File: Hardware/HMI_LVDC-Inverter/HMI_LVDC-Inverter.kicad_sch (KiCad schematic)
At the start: 1 part, among them J10 Conn_01x06_Pin

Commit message: Terminado el esquemático del HMI
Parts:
- removed J10: Conn_01x06_Pin, symbol Connector:Conn_01x06_Pin
- added J1: Conn_01x02, Connector_Hirose:Hirose_DF13-02P-1.25DS_1x02_P1.25mm_Horizontal, symbol Connector_Generic:Conn_01x02
- added J2: Conn_01x09_Pin, Connector_Phoenix_SPT:PhoenixContact_SPT_2.5_9-V-5.0-EX_1x09_P5.0mm_Vertical, symbol Connector:Conn_01x09_Pin
- added J3, J4, J5: Conn_01x05, Connector_PinHeader_1.00mm:PinHeader_1x05_P1.00mm_Vertical, symbol Connector_Generic:Conn_01x05
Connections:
- net GND: now also J3.5 (Pin_5), J4.2 (Pin_2), J5.1 (Pin_1)
- new net +12V_ISO: J1.1 (Pin_1)
- new net +3.3V: J4.5 (Pin_5)
- new net +5V: J4.1 (Pin_1)
- new net GND_ISO: J1.2 (Pin_2)
- new net MCU/ESP_EN: J3.3 (Pin_3)
- new net MCU/ESP_PROG: J3.4 (Pin_4)
- new net MCU/MISO: J5.4 (Pin_4)
- new net MCU/MOSI: J5.5 (Pin_5)
- new net MCU/NSS: J5.2 (Pin_2)
- new net MCU/RXD0_prog: J3.1 (Pin_1)
- new net MCU/SCK: J5.3 (Pin_3)
- new net MCU/TXD0_prog: J3.2 (Pin_2)
- new net MCU/VSens_Corriente: J4.3 (Pin_3)
- new net MCU/Vsens_HV: J4.4 (Pin_4)
- new net Perifericos/FREQ_SEL_1_ISO: J2.6 (Pin_6)
- new net Perifericos/FREQ_SEL_2_ISO: J2.5 (Pin_5)
- new net Perifericos/FREQ_SEL_3_ISO: J2.4 (Pin_4)
- new net Perifericos/FREQ_SEL_4_ISO: J2.3 (Pin_3)
- new net Perifericos/RELAY_COM: J2.8 (Pin_8)
- new net Perifericos/RELAY_NC: J2.7 (Pin_7)
- new net Perifericos/RELAY_NO: J2.9 (Pin_9)
- new net Perifericos/START_CTRL_ISO: J2.2 (Pin_2)
- new net Perifericos/STOP_BUTTON_ISO: J2.1 (Pin_1)
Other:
- sheet Fuentes ports: added none; removed 12V_test
- sheet MCU ports: added ESP_EN, ESP_PROG, FREQ_SEL_1, FREQ_SEL_2, FREQ_SEL_3, FREQ_SEL_4, MISO, MOSI, NSS, RELAY_CTRL, RXD0_prog, SCK, START_CTRL, STOP_BUTTON, TXD0_prog, V0-10V, VSens_Corriente, Vsens_HV; removed 12V_test, Inv_Rx, Inv_Tx, Touch_0, Touch_1, Touch_2, Touch_3, Touch_4, Touch_5
- sheet Perifericos ports: added FREQ_SEL_1, FREQ_SEL_1_ISO, FREQ_SEL_2, FREQ_SEL_2_ISO, FREQ_SEL_3, FREQ_SEL_3_ISO, FREQ_SEL_4, FREQ_SEL_4_ISO, RELAY_COM, RELAY_CTRL, RELAY_NC, RELAY_NO, START_CTRL, START_CTRL_ISO, STOP_BUTTON, STOP_BUTTON_ISO, V0-10V; removed Touch_0, Touch_1, Touch_2, Touch_3, Touch_4, Touch_5
- note added: "CONECTORES CON INVERTER"
- note removed: "CONECTOR CON INVERTER"

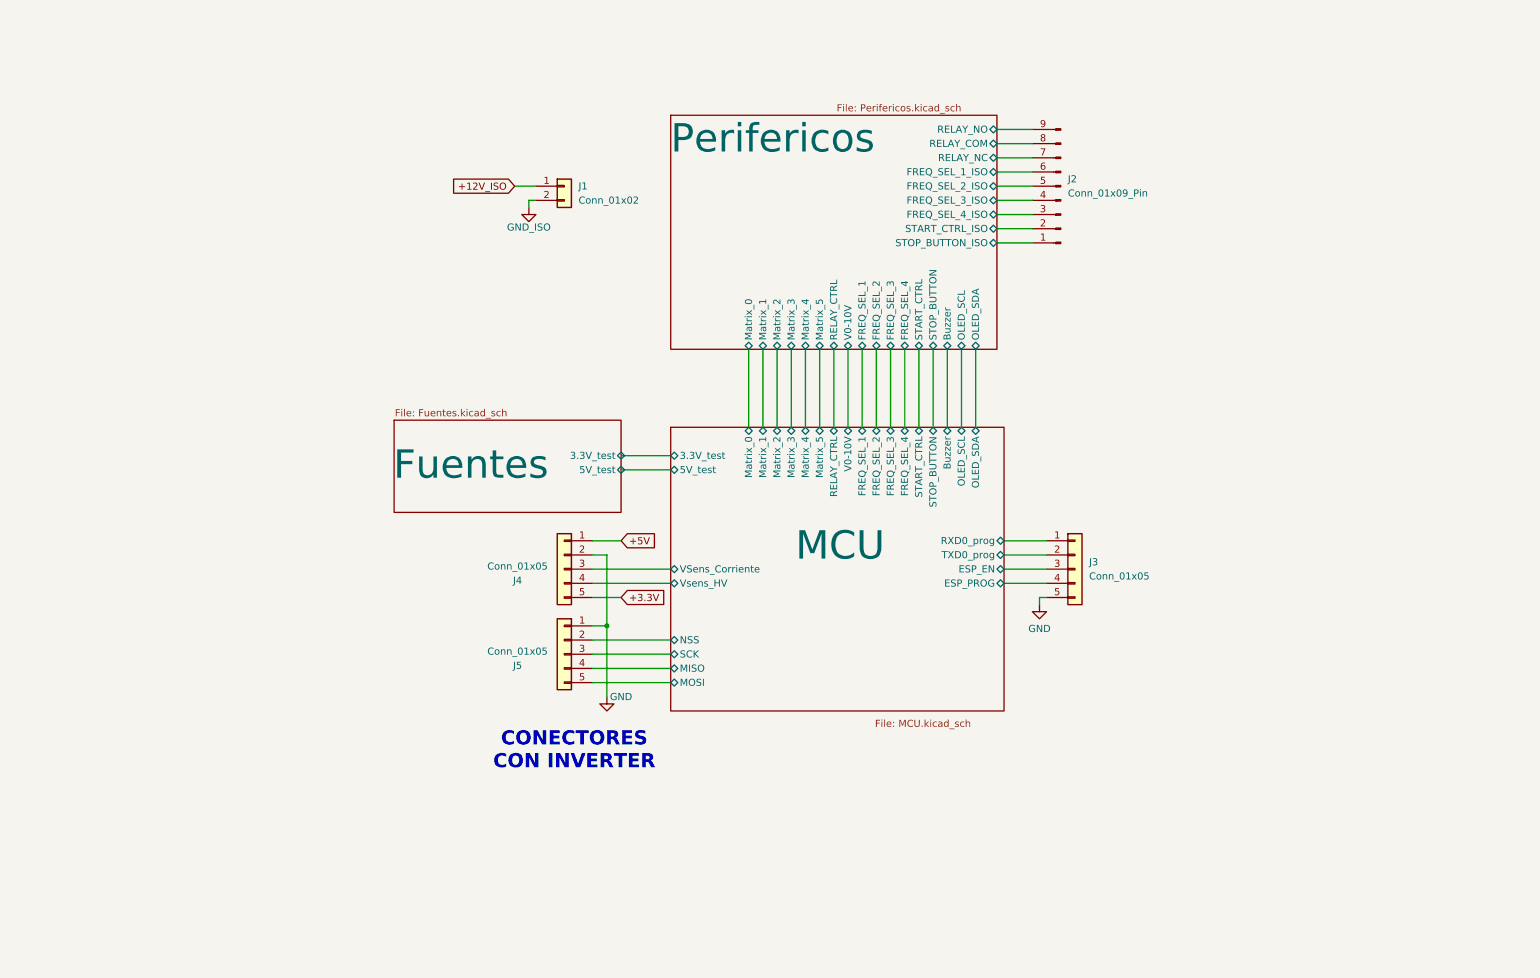
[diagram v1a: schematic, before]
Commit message: Avance con el esquemático, faltan definir algunas etiquetas que no las encontré
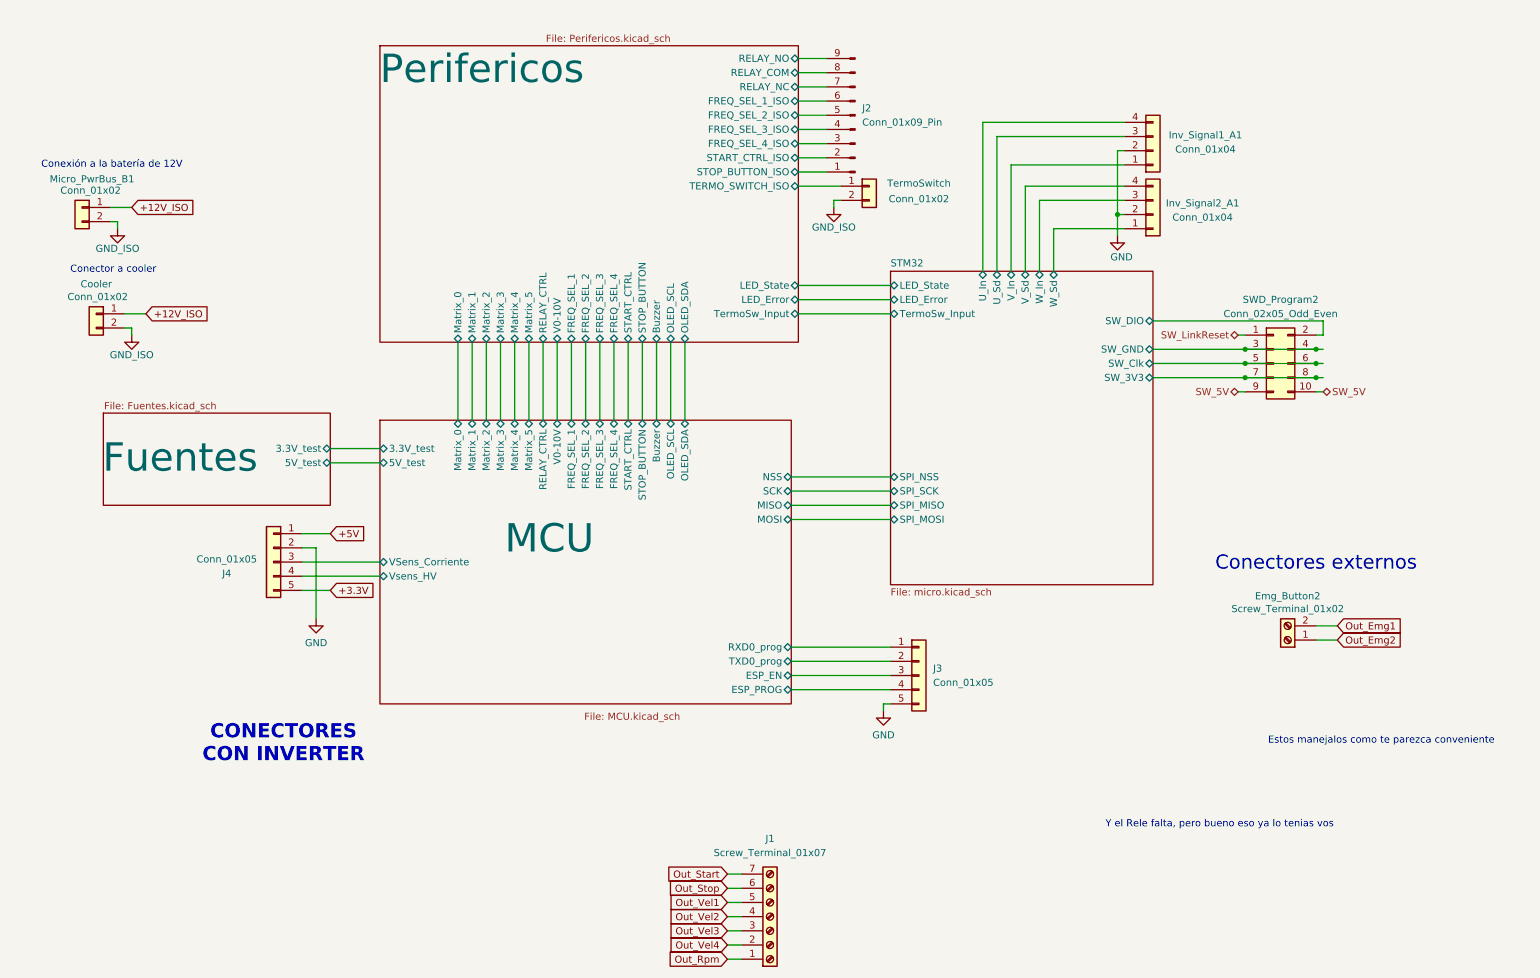
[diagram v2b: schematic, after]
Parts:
- removed J1: Conn_01x02, Connector_Hirose:Hirose_DF13-02P-1.25DS_1x02_P1.25mm_Horizontal, symbol Connector_Generic:Conn_01x02
- removed J5: Conn_01x05, Connector_PinHeader_1.00mm:PinHeader_1x05_P1.00mm_Vertical, symbol Connector_Generic:Conn_01x05
- added Cooler, TermoSwitch: Conn_01x02, Connector_Molex:Molex_KK-254_AE-6410-02A_1x02_P2.54mm_Vertical, symbol Connector_Generic:Conn_01x02
- added Emg_Button2: Screw_Terminal_01x02, TerminalBlock_Phoenix:TerminalBlock_Phoenix_MKDS-1,5-2_1x02_P5.00mm_Horizontal, symbol Connector:Screw_Terminal_01x02
- added Inv_Signal1_A1, Inv_Signal2_A1: Conn_01x04, Connector_Molex:Molex_KK-254_AE-6410-04A_1x04_P2.54mm_Vertical, symbol Connector_Generic:Conn_01x04
- added J1: Screw_Terminal_01x07, TerminalBlock_Phoenix:TerminalBlock_Phoenix_PT-1,5-7-5.0-H_1x07_P5.00mm_Horizontal, symbol Connector:Screw_Terminal_01x07
- added Micro_PwrBus_B1: Conn_01x02, Connector_Phoenix_MSTB:PhoenixContact_MSTBVA_2,5_2-G-5,08_1x02_P5.08mm_Vertical, symbol Connector_Generic:Conn_01x02
- added SWD_Program2: Conn_02x05_Odd_Even, Connector_IDC:IDC-Header_2x05_P2.54mm_Vertical_SMD, symbol Connector_Generic:Conn_02x05_Odd_Even
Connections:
- net +12V_ISO: now also Cooler.1 (Pin_1), Micro_PwrBus_B1.1 (Pin_1)
- net GND: now also Inv_Signal1_A1.2 (Pin_2), Inv_Signal2_A1.2 (Pin_2)
- net GND_ISO: now also Cooler.2 (Pin_2), Micro_PwrBus_B1.2 (Pin_2), TermoSwitch.2 (Pin_2)
- new net Out_Emg1: Emg_Button2.2 (Pin_2)
- new net Out_Emg2: Emg_Button2.1 (Pin_1)
- new net Out_Rpm: J1.1 (Pin_1)
- new net Out_Start: J1.7 (Pin_7)
- new net Out_Stop: J1.6 (Pin_6)
- new net Out_Vel1: J1.5 (Pin_5)
- new net Out_Vel2: J1.4 (Pin_4)
- new net Out_Vel3: J1.3 (Pin_3)
- new net Out_Vel4: J1.2 (Pin_2)
- new net Perifericos/TERMO_SWITCH_ISO: TermoSwitch.1 (Pin_1)
- new net STM32/SW_3V3: SWD_Program2.7 (Pin_7), SWD_Program2.8 (Pin_8)
- new net STM32/SW_Clk: SWD_Program2.5 (Pin_5), SWD_Program2.6 (Pin_6)
- new net STM32/SW_DIO: SWD_Program2.2 (Pin_2)
- new net STM32/SW_GND: SWD_Program2.3 (Pin_3), SWD_Program2.4 (Pin_4)
- new net STM32/U_In: Inv_Signal1_A1.4 (Pin_4)
- new net STM32/U_Sd: Inv_Signal1_A1.3 (Pin_3)
- new net STM32/V_In: Inv_Signal1_A1.1 (Pin_1)
- new net STM32/V_Sd: Inv_Signal2_A1.4 (Pin_4)
- new net STM32/W_In: Inv_Signal2_A1.3 (Pin_3)
- new net STM32/W_Sd: Inv_Signal2_A1.1 (Pin_1)
- new net SW_5V: SWD_Program2.10 (Pin_10), SWD_Program2.9 (Pin_9)
- new net SW_LinkReset: SWD_Program2.1 (Pin_1)
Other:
- added sheet STM32 (micro.kicad_sch)
- sheet Perifericos ports: added LED_Error, LED_State, TERMO_SWITCH_ISO, TermoSw_Input; removed none
- note added: "Conector a cooler"
- note added: "Conectores externos"
- note added: "Conexión a la batería de 12V"
- note added: "Estos manejalos como te parezca conveniente"
- note added: "Y el Rele falta, pero bueno eso ya lo tenias vos"
- moved on the sheet: J2, J3, J4

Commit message: Terminado todo el conexionado eléctrico esquemático
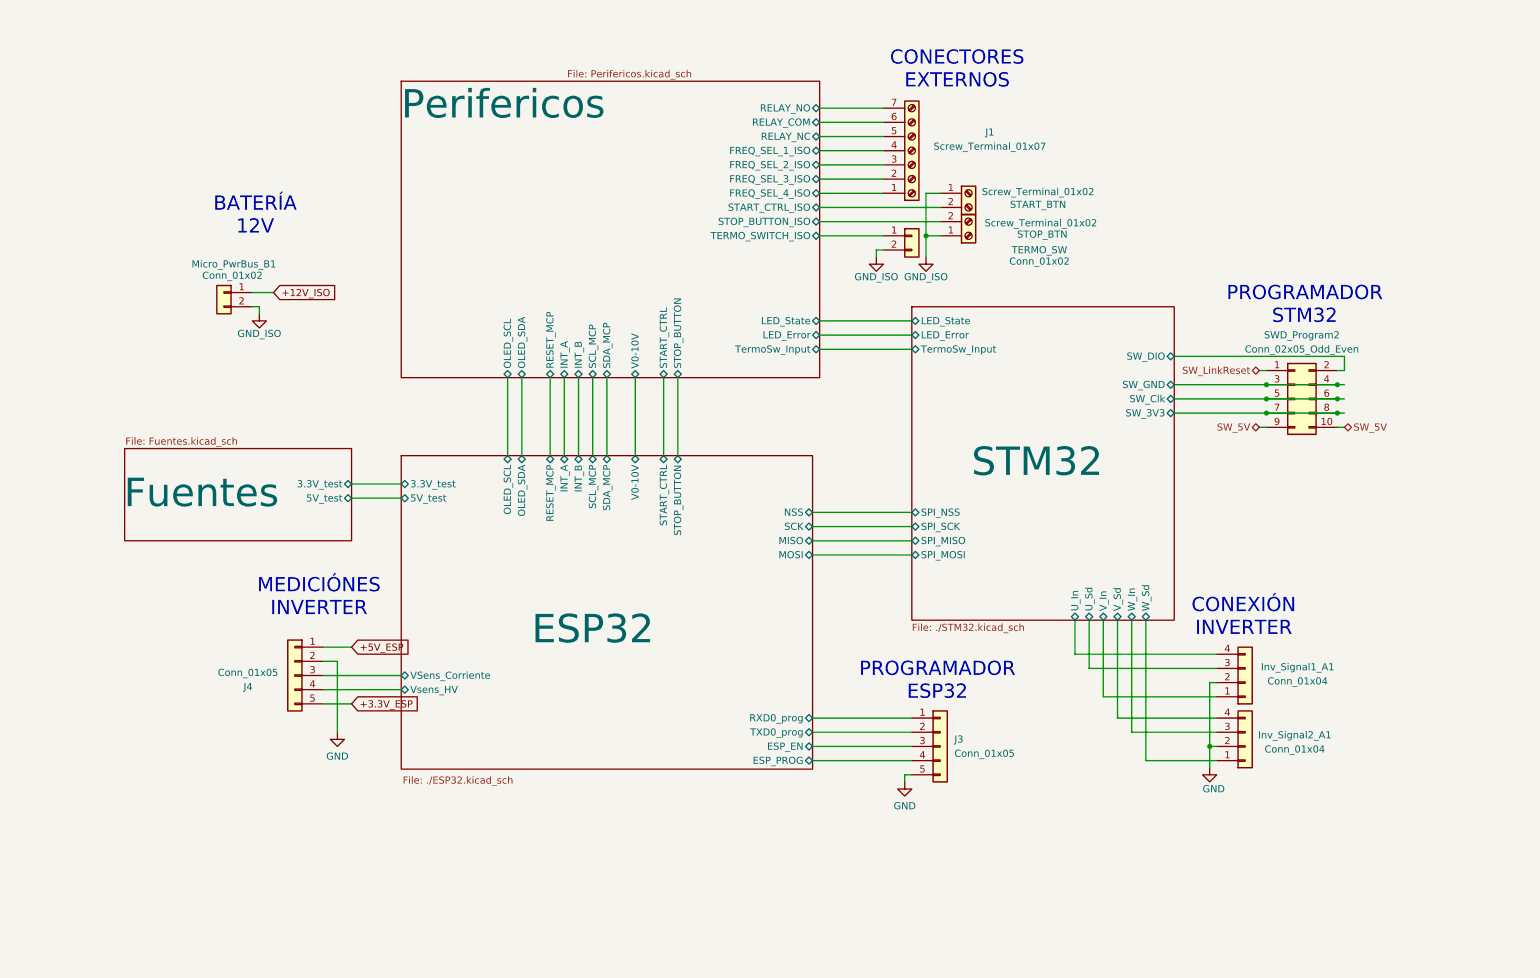
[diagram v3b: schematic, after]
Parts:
- removed Cooler: Conn_01x02, Connector_Molex:Molex_KK-254_AE-6410-02A_1x02_P2.54mm_Vertical, symbol Connector_Generic:Conn_01x02
- removed J2: Conn_01x09_Pin, Connector_Phoenix_SPT:PhoenixContact_SPT_2.5_9-V-5.0-EX_1x09_P5.0mm_Vertical, symbol Connector:Conn_01x09_Pin
- added STOP_BTN: Screw_Terminal_01x02, TerminalBlock_Phoenix:TerminalBlock_Phoenix_MKDS-1,5-2_1x02_P5.00mm_Horizontal, symbol Connector:Screw_Terminal_01x02
- renumbered Emg_Button2 to START_BTN, TermoSwitch to TERMO_SW
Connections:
- net Out_Emg1 is gone; now on net Perifericos/START_CTRL_ISO: START_BTN.2 (Pin_2)
- net Out_Emg2 is gone; now on net GND_ISO: START_BTN.1 (Pin_1)
- net Out_Rpm is gone; now on net Perifericos/FREQ_SEL_4_ISO: J1.1 (Pin_1)
- net Out_Start is gone; now on net Perifericos/RELAY_NO: J1.7 (Pin_7)
- net Out_Stop is gone; now on net Perifericos/RELAY_COM: J1.6 (Pin_6)
- net Out_Vel1 is gone; now on net Perifericos/RELAY_NC: J1.5 (Pin_5)
- net Out_Vel2 is gone; now on net Perifericos/FREQ_SEL_1_ISO: J1.4 (Pin_4)
- net Out_Vel3 is gone; now on net Perifericos/FREQ_SEL_2_ISO: J1.3 (Pin_3)
- net Out_Vel4 is gone; now on net Perifericos/FREQ_SEL_3_ISO: J1.2 (Pin_2)
- net GND_ISO: now also STOP_BTN.1 (Pin_1)
- net Perifericos/STOP_BUTTON_ISO: now also STOP_BTN.2 (Pin_2)
- net +3.3V renamed +3.3V_ESP
- net +5V renamed +5V_ESP
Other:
- sheet MCU renamed ESP32
- sheet ESP32: file MCU.kicad_sch -> ./ESP32.kicad_sch
- sheet ESP32 ports: added INT_A, INT_B, RESET_MCP, SCL_MCP, SDA_MCP; removed Buzzer, FREQ_SEL_1, FREQ_SEL_2, FREQ_SEL_3, FREQ_SEL_4, Matrix_0, Matrix_1, Matrix_2, Matrix_3, Matrix_4, Matrix_5, RELAY_CTRL
- sheet Perifericos ports: added INT_A, INT_B, RESET_MCP, SCL_MCP, SDA_MCP; removed Buzzer, FREQ_SEL_1, FREQ_SEL_2, FREQ_SEL_3, FREQ_SEL_4, Matrix_0, Matrix_1, Matrix_2, Matrix_3, Matrix_4, Matrix_5, RELAY_CTRL
- sheet STM32: file micro.kicad_sch -> ./STM32.kicad_sch
- note added: "BATERÍA 12V"
- note added: "CONECTORES EXTERNOS"
- note added: "CONEXIÓN INVERTER"
- note added: "MEDICIÓNES INVERTER"
- note added: "PROGRAMADOR ESP32"
- note added: "PROGRAMADOR STM32"
- note removed: "CONECTORES CON INVERTER"
- note removed: "Conector a cooler"
- note removed: "Conectores externos"
- note removed: "Conexión a la batería de 12V"
- note removed: "Estos manejalos como te parezca conveniente"
- note removed: "Y el Rele falta, pero bueno eso ya lo tenias vos"
- company: (none) -> Andrenacci - Carra
- title: (none) -> Variador de frecuencia LVDC
- moved on the sheet: Inv_Signal1_A1, Inv_Signal2_A1, J1, J3, J4, Micro_PwrBus_B1, START_BTN, SWD_Program2, TERMO_SW

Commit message: Agregado de los componentes con links de compra en KiCAD a excepción de los conectores
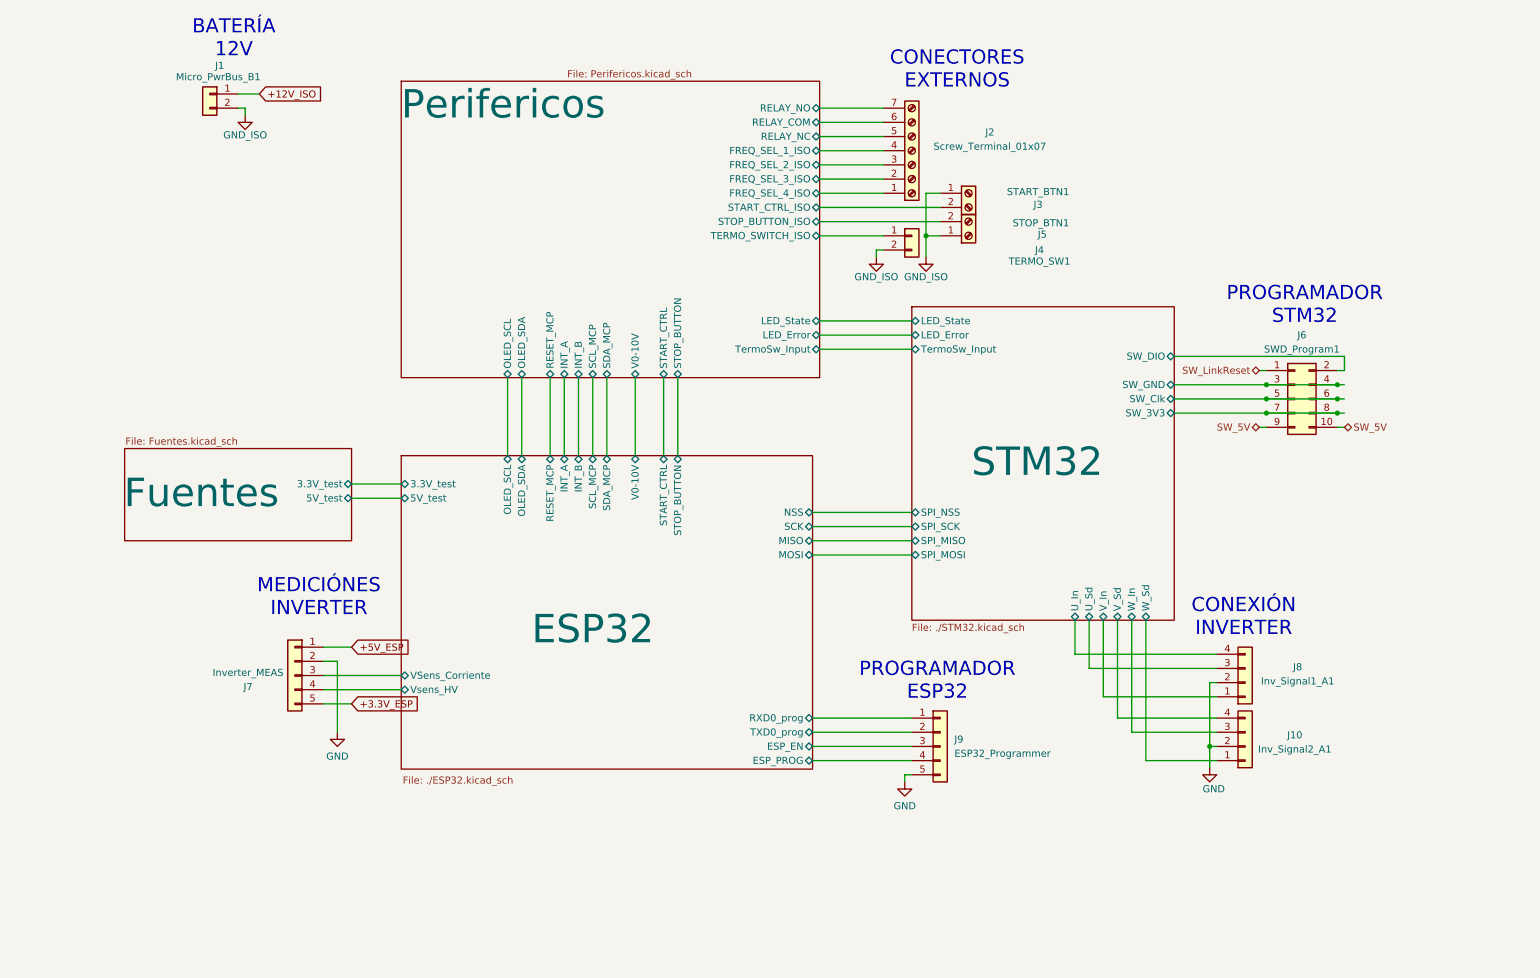
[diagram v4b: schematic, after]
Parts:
- J1: renamed from Micro_PwrBus_B1; value Conn_01x02 -> Micro_PwrBus_B1
- J10: renamed from Inv_Signal2_A1; value Conn_01x04 -> Inv_Signal2_A1
- J3: renamed from START_BTN; value Screw_Terminal_01x02 -> START_BTN1
- J4: renamed from TERMO_SW; value Conn_01x02 -> TERMO_SW1
- J5: renamed from STOP_BTN; value Screw_Terminal_01x02 -> STOP_BTN1
- J6: renamed from SWD_Program2; value Conn_02x05_Odd_Even -> SWD_Program1
- J7: renamed from J4; value Conn_01x05 -> Inverter_MEAS
- J8: renamed from Inv_Signal1_A1; value Conn_01x04 -> Inv_Signal1_A1
- J9: renamed from J3; value Conn_01x05 -> ESP32_Programmer
- renumbered J1 to J2
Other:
- moved on the sheet: J1
